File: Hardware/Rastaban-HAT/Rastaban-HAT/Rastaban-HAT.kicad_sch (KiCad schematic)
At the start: 59 parts, among them IC1 P82B96TD,118, J1 Screw_Terminal_01x04, J10 GPIO, J11 Conn_01x06_Male, J2 Screw_Terminal_01x04, J3 Screw_Terminal_01x04, J4 Screw_Terminal_01x02, J5 Jack-DC 12V+, J6 SM04B-SRSS-TB(LF)(SN), J7 Screw_Terminal_01x02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

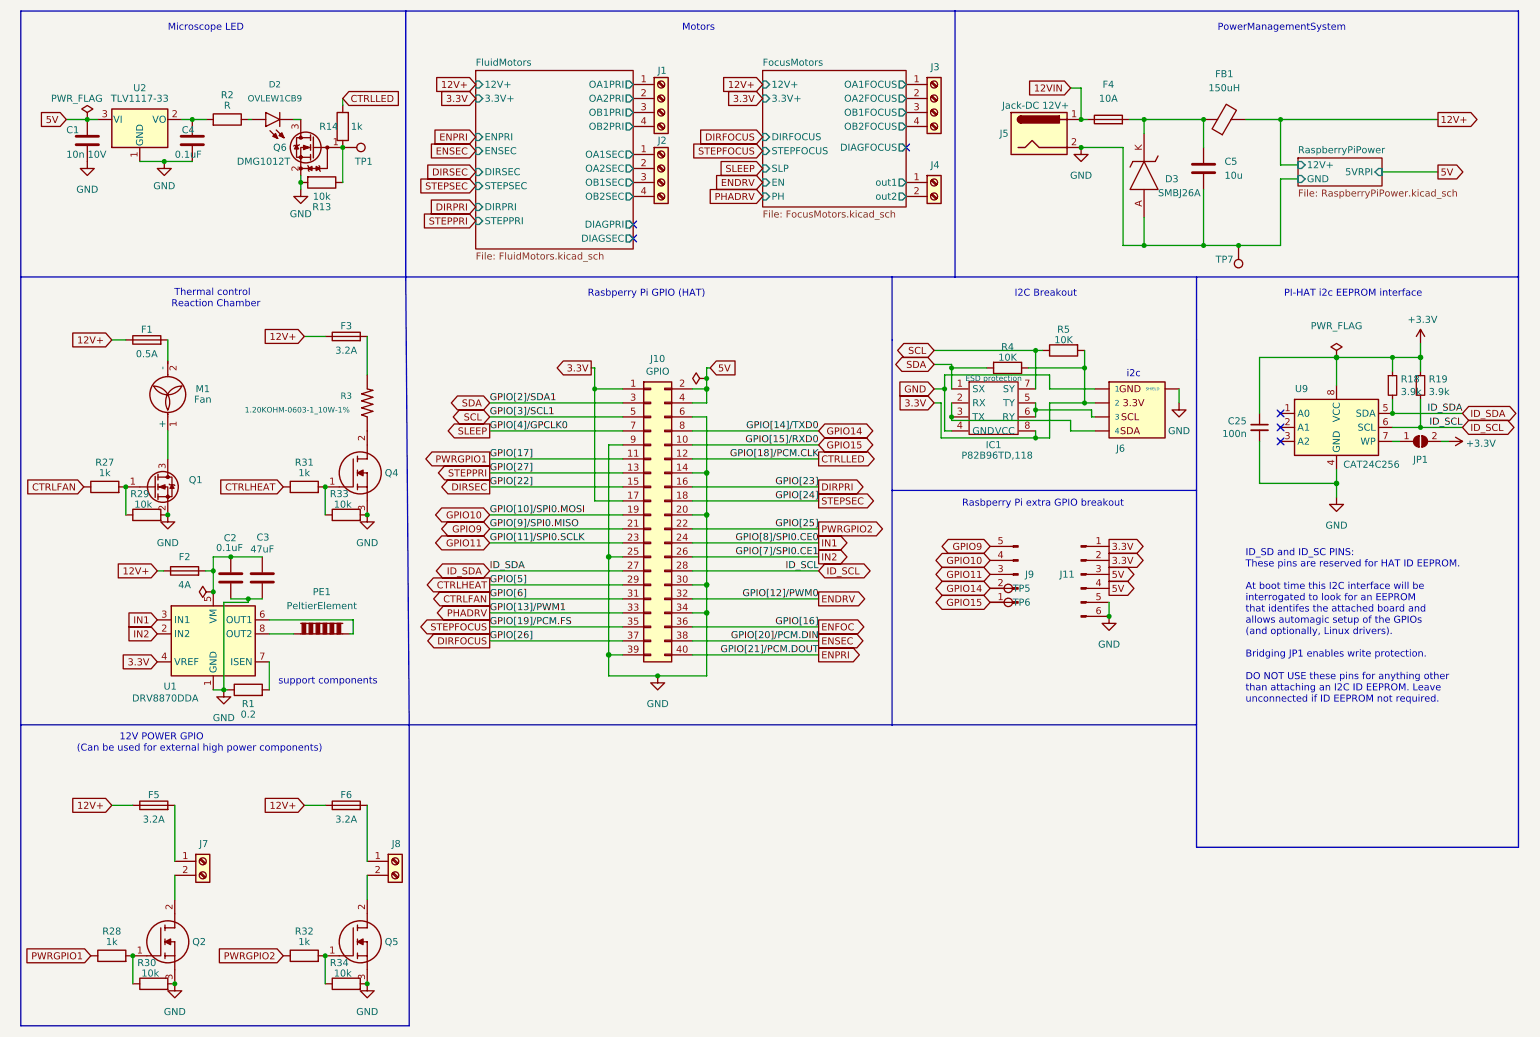
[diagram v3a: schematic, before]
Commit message: changed revision to v1.1 on all tabs
changed some capacitor values
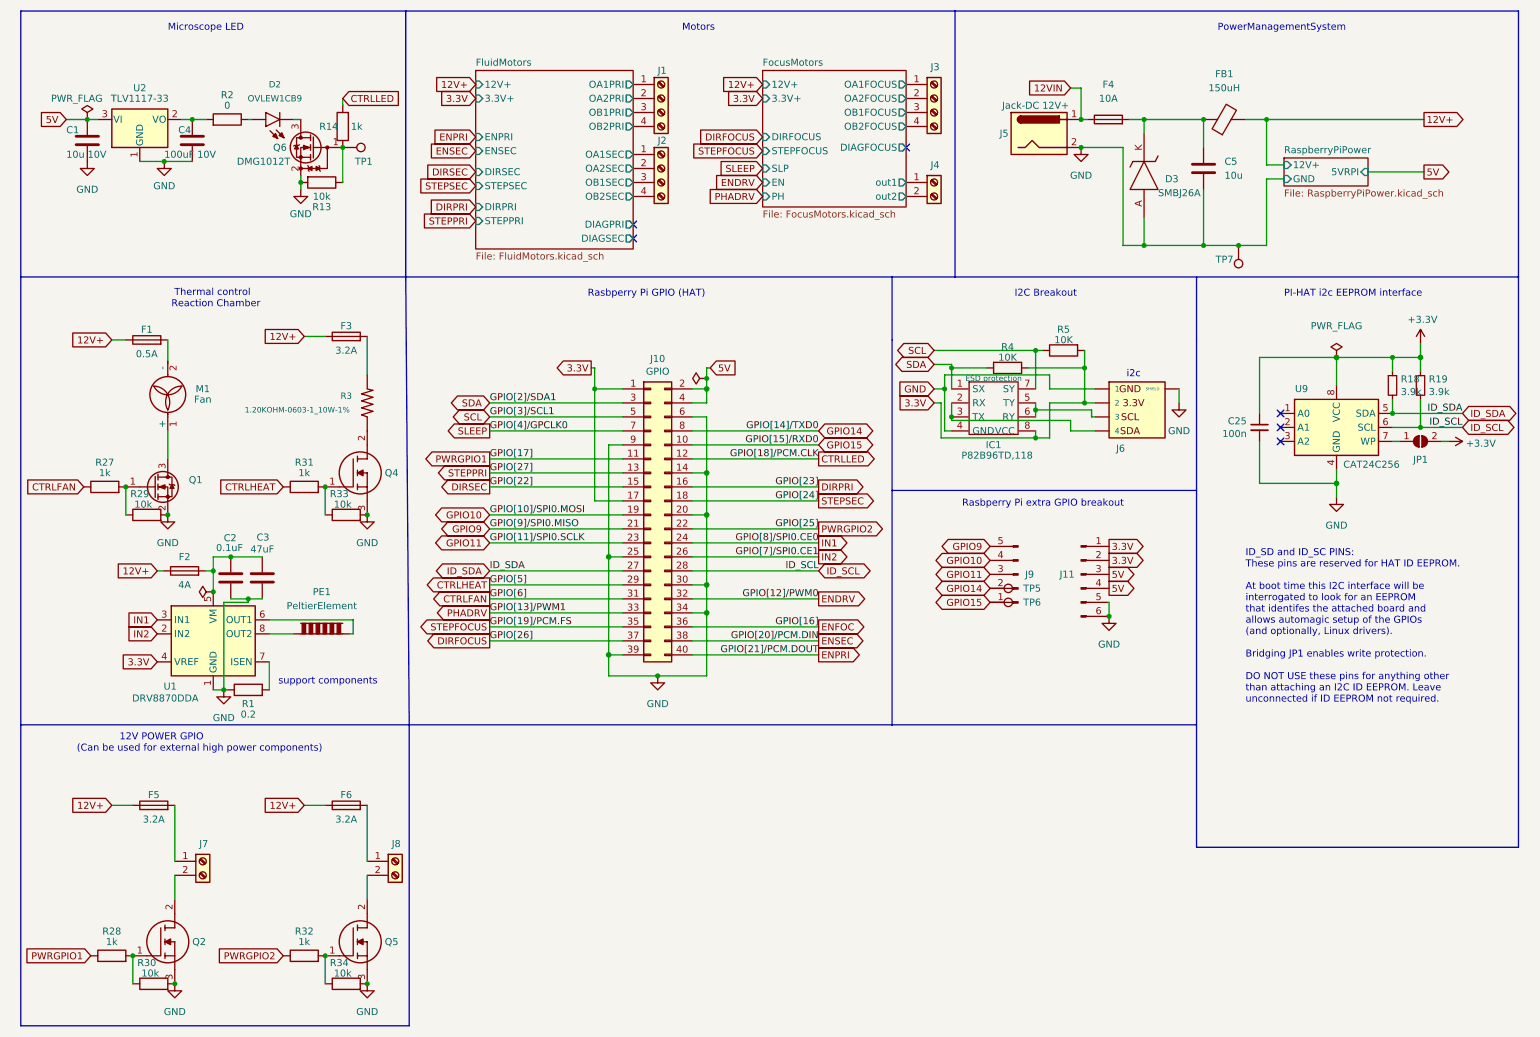
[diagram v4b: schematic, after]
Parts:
- C1: value 10n 10V -> 10u 10V
- C4: value 0.1uF -> 100uF 10V
- R2: value R -> 0
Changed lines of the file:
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@@
     (title "Rastaban-HAT")
     (date "2022-09-21")
-    (rev "1")
+    (rev "1.1")
     (company "HAN")
     (comment 1 "Casper R. Tak")
@@
   (junction (at 196.85 90.17) (diameter 0) (color 0 0 0 0)
   )
-  (junction (at 241.3 32.385) (diameter 0) (color 0 0 0 0)
+  (junction (at 238.76 32.385) (diameter 0) (color 0 0 0 0)
   )
   (junction (at 261.62 85.725) (diameter 0) (color 0 0 0 0)
@@
     (stroke (width 0) (type solid) (color 0 0 0 0))
   )
-  (wire (pts (xy 259.715 41.91) (xy 269.875 41.91))
+  (wire (pts (xy 257.175 41.91) (xy 267.335 41.91))
     (stroke (width 0) (type default) (color 0 0 0 0))
   )
@@
     (stroke (width 0) (type default) (color 0 0 0 0))
   )
-  (wire (pts (xy 241.3 43.18) (xy 244.475 43.18))
+  (wire (pts (xy 238.76 43.18) (xy 241.935 43.18))
     (stroke (width 0) (type default) (color 0 0 0 0))
   )
@@
     (stroke (width 0) (type default) (color 0 0 0 0))
   )
-  (wire (pts (xy 241.3 32.385) (xy 269.875 32.385))
+  (wire (pts (xy 238.76 32.385) (xy 267.335 32.385))
     (stroke (width 0) (type default) (color 0 0 0 0))
   )
@@
     (stroke (width 0) (type default) (color 0 0 0 0))
   )
+  (wire (pts (xy 234.95 32.385) (xy 238.76 32.385))
+    (stroke (width 0) (type default) (color 0 0 0 0))
+  )
   (wire (pts (xy 47.625 135.89) (xy 49.53 135.89))
     (stroke (width 0) (type default) (color 0 0 0 0))
@@
     (stroke (width 0) (type default) (color 0 0 0 0))
   )
-  (wire (pts (xy 233.68 55.245) (xy 241.3 55.245))
-    (stroke (width 0) (type default) (color 0 0 0 0))
-  )
   (wire (pts (xy 116.84 81.28) (xy 116.84 101.6))
     (stroke (width 0) (type solid) (color 0 0 0 0))
@@
     (stroke (width 0) (type default) (color 0 0 0 0))
   )
-  (wire (pts (xy 241.3 40.64) (xy 241.3 32.385))
+  (wire (pts (xy 238.76 40.64) (xy 238.76 32.385))
     (stroke (width 0) (type default) (color 0 0 0 0))
   )
@@
     (stroke (width 0) (type solid) (color 0 0 0 0))
   )
-  (wire (pts (xy 244.475 40.64) (xy 241.3 40.64))
+  (wire (pts (xy 241.935 40.64) (xy 238.76 40.64))
     (stroke (width 0) (type default) (color 0 0 0 0))
   )
@@
     (stroke (width 0) (type solid) (color 0 0 0 0))
   )
-  (wire (pts (xy 234.95 32.385) (xy 241.3 32.385))
-    (stroke (width 0) (type default) (color 0 0 0 0))
-  )
   (wire (pts (xy 119.38 133.35) (xy 128.27 133.35))
     (stroke (width 0) (type default) (color 0 0 0 0))
@@
     (stroke (width 0) (type solid) (color 0 0 0 0))
   )
+  (wire (pts (xy 233.68 55.245) (xy 238.76 55.245))
+    (stroke (width 0) (type default) (color 0 0 0 0))
+  )
   (polyline (pts (xy 12.7 12.7) (xy 12.7 60.96))
     (stroke (width 0) (type default) (color 0 0 0 0))
@@
     (stroke (width 0) (type solid) (color 0 0 0 0))
   )
+  (wire (pts (xy 227.33 55.245) (xy 233.68 55.245))
+    (stroke (width 0) (type default) (color 0 0 0 0))
+  )
   (wire (pts (xy 178.435 83.82) (xy 179.705 83.82))
     (stroke (width 0) (type default) (color 0 0 0 0))
@@
     (stroke (width 0) (type default) (color 0 0 0 0))
   )
-  (wire (pts (xy 227.33 55.245) (xy 233.68 55.245))
-    (stroke (width 0) (type default) (color 0 0 0 0))
-  )
   (wire (pts (xy 63.5 43.815) (xy 63.5 45.085))
     (stroke (width 0) (type default) (color 0 0 0 0))
@@
     (stroke (width 0) (type solid) (color 0 0 0 0))
   )
-  (wire (pts (xy 241.3 55.245) (xy 241.3 43.18))
+  (wire (pts (xy 238.76 55.245) (xy 238.76 43.18))
     (stroke (width 0) (type default) (color 0 0 0 0))
   )
@@
     )
   )
-  (global_label "5V" (shape output) (at 269.875 41.91 0) (fields_autoplaced)
+  (global_label "5V" (shape output) (at 267.335 41.91 0) (fields_autoplaced)
     (effects (font (size 1.27 1.27)) (justify left))
-    (property "Intersheet References" "${INTERSHEET_REFS}" (id 0) (at 274.5862 41.8306 0)
+    (property "Intersheet References" "${INTERSHEET_REFS}" (id 0) (at 272.0462 41.8306 0)
       (effects (font (size 1.27 1.27)) (justify left) hide)
     )
@@
     )
   )
-  (global_label "12V+" (shape output) (at 269.875 32.385 0) (fields_autoplaced)
+  (global_label "12V+" (shape output) (at 267.335 32.385 0) (fields_autoplaced)
     (effects (font (size 1.27 1.27)) (justify left))
-    (property "Intersheet References" "${INTERSHEET_REFS}" (id 0) (at 277.3681 32.3056 0)
+    (property "Intersheet References" "${INTERSHEET_REFS}" (id 0) (at 274.8281 32.3056 0)
       (effects (font (size 1.27 1.27)) (justify left) hide)
     )
@@
     (in_bom yes) (on_board yes)
     (property "Reference" "R2" (id 0) (at 50.165 27.94 90))
-    (property "Value" "R" (id 1) (at 50.165 29.845 90))
+    (property "Value" "0" (id 1) (at 50.165 29.845 90))
     (property "Footprint" "" (id 2) (at 50.165 34.163 90)
       (effects (font (size 1.27 1.27)) hide)
@@
   (symbol (lib_id "Connector:TestPoint") (at 188.595 117.475 270) (unit 1)
     (in_bom yes) (on_board yes)
-    (property "Reference" "TP5" (id 0) (at 194.31 117.475 90))
+    (property "Reference" "TP5" (id 0) (at 196.215 117.475 90))
     (property "Value" "TestPoint" (id 1) (at 193.675 117.475 0)
       (effects (font (size 1.27 1.27)) hide)
@@
   (symbol (lib_id "Connector:TestPoint") (at 188.595 120.015 270) (unit 1)
     (in_bom yes) (on_board yes)
-    (property "Reference" "TP6" (id 0) (at 194.31 120.015 90))
+    (property "Reference" "TP6" (id 0) (at 196.215 120.015 90))
     (property "Value" "TestPoint" (id 1) (at 193.675 120.015 0)
       (effects (font (size 1.27 1.27)) hide)
@@
   (symbol (lib_id "Device:C") (at 43.815 36.195 180) (unit 1)
     (in_bom yes) (on_board yes)
-    (property "Reference" "C4" (id 0) (at 41.91 34.29 0)
+    (property "Reference" "C4" (id 0) (at 41.275 34.29 0)
       (effects (font (size 1.27 1.27)) (justify right))
     )
-    (property "Value" "0.1uF" (id 1) (at 40.64 38.735 0)
+    (property "Value" "100uF 10V" (id 1) (at 38.735 38.735 0)
       (effects (font (size 1.27 1.27)) (justify right))
     )
@@
       (effects (font (size 1.27 1.27)) (justify left))
     )
-    (property "Value" "10n 10V" (id 1) (at 20.955 38.735 0)
+    (property "Value" "10u 10V" (id 1) (at 20.955 38.735 0)
       (effects (font (size 1.27 1.27)) (justify left))
     )
@@
     )
   )
-  (sheet (at 244.475 39.37) (size 15.24 5.08) (fields_autoplaced)
+  (sheet (at 241.935 39.37) (size 15.24 5.08) (fields_autoplaced)
     (stroke (width 0.1524) (type solid) (color 0 0 0 0))
     (fill (color 0 0 0 0.0000))
-    (property "Sheet name" "RaspberryPiPower" (id 0) (at 244.475 38.6584 0)
+    (property "Sheet name" "RaspberryPiPower" (id 0) (at 241.935 38.6584 0)
       (effects (font (size 1.27 1.27)) (justify left bottom))
     )
-    (property "Sheet file" "RaspberryPiPower.kicad_sch" (id 1) (at 244.475 45.0346 0)
+    (property "Sheet file" "RaspberryPiPower.kicad_sch" (id 1) (at 241.935 45.0346 0)
       (effects (font (size 1.27 1.27)) (justify left top))
     )
-    (pin "12V+" input (at 244.475 40.64 180)
+    (pin "12V+" input (at 241.935 40.64 180)
       (effects (font (size 1.27 1.27)) (justify left))
     )
-    (pin "GND" input (at 244.475 43.18 180)
+    (pin "GND" input (at 241.935 43.18 180)
       (effects (font (size 1.27 1.27)) (justify left))
     )
-    (pin "5VRPI" input (at 259.715 41.91 0)
+    (pin "5VRPI" input (at 257.175 41.91 0)
       (effects (font (size 1.27 1.27)) (justify right))
     )
@@
     )
     (path "/f3fe5026-3ec3-4ef9-8ee4-ac53381f5d3c"
-      (reference "C1") (unit 1) (value "10n 10V") (footprint "")
+      (reference "C1") (unit 1) (value "10u 10V") (footprint "")
     )
     (path "/6e705e76-606c-4ed6-ae7f-ed966b630818"
@@
     )
     (path "/9f7db502-d21d-4e3f-97d2-a5c274cc55fe"
-      (reference "C4") (unit 1) (value "0.1uF") (footprint "Capacitor_SMD:C_1206_3216Metric_Pad1.33x1.80mm_HandSolder")
+      (reference "C4") (unit 1) (value "100uF 10V") (footprint "Capacitor_SMD:C_1206_3216Metric_Pad1.33x1.80mm_HandSolder")
     )
     (path "/bf4c234e-8821-4f3f-91ed-c4127b83d67d"
@@
     )
     (path "/509754cd-dbf1-46e6-965c-38d41c0b6924/b391f05e-9d79-4808-8c88-d0da93b38ae2"
-      (reference "C16") (unit 1) (value "100n 35V") (footprint "")
+      (reference "C16") (unit 1) (value "100u 35V") (footprint "")
     )
     (path "/509754cd-dbf1-46e6-965c-38d41c0b6924/e00c426b-f72a-4212-94e0-d9ce7621402d"
-      (reference "C17") (unit 1) (value "100n 35V") (footprint "")
+      (reference "C17") (unit 1) (value "100u 35V") (footprint "")
     )
     (path "/7b03732c-6b0a-482e-b8e3-ced6ad7436b5/6a92e50c-ed6c-499b-95da-e3221c59e174"
@@
     )
     (path "/7b03732c-6b0a-482e-b8e3-ced6ad7436b5/e5d64b5c-b610-4e2e-9355-8b38ef775df4"
-      (reference "C19") (unit 1) (value "10n 10V") (footprint "")
+      (reference "C19") (unit 1) (value "10u 10V") (footprint "")
     )
     (path "/6d1772b3-b434-4c39-820a-75c27b63c8e3"
@@
     )
     (path "/00db92f9-b335-411c-b323-c06099a8c80d"
-      (reference "R2") (unit 1) (value "R") (footprint "")
+      (reference "R2") (unit 1) (value "0") (footprint "")
     )
     (path "/e2569925-ebf9-4052-bd02-8582502d3183"

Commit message: Heavily improved symbol text placements
all texts are now readable
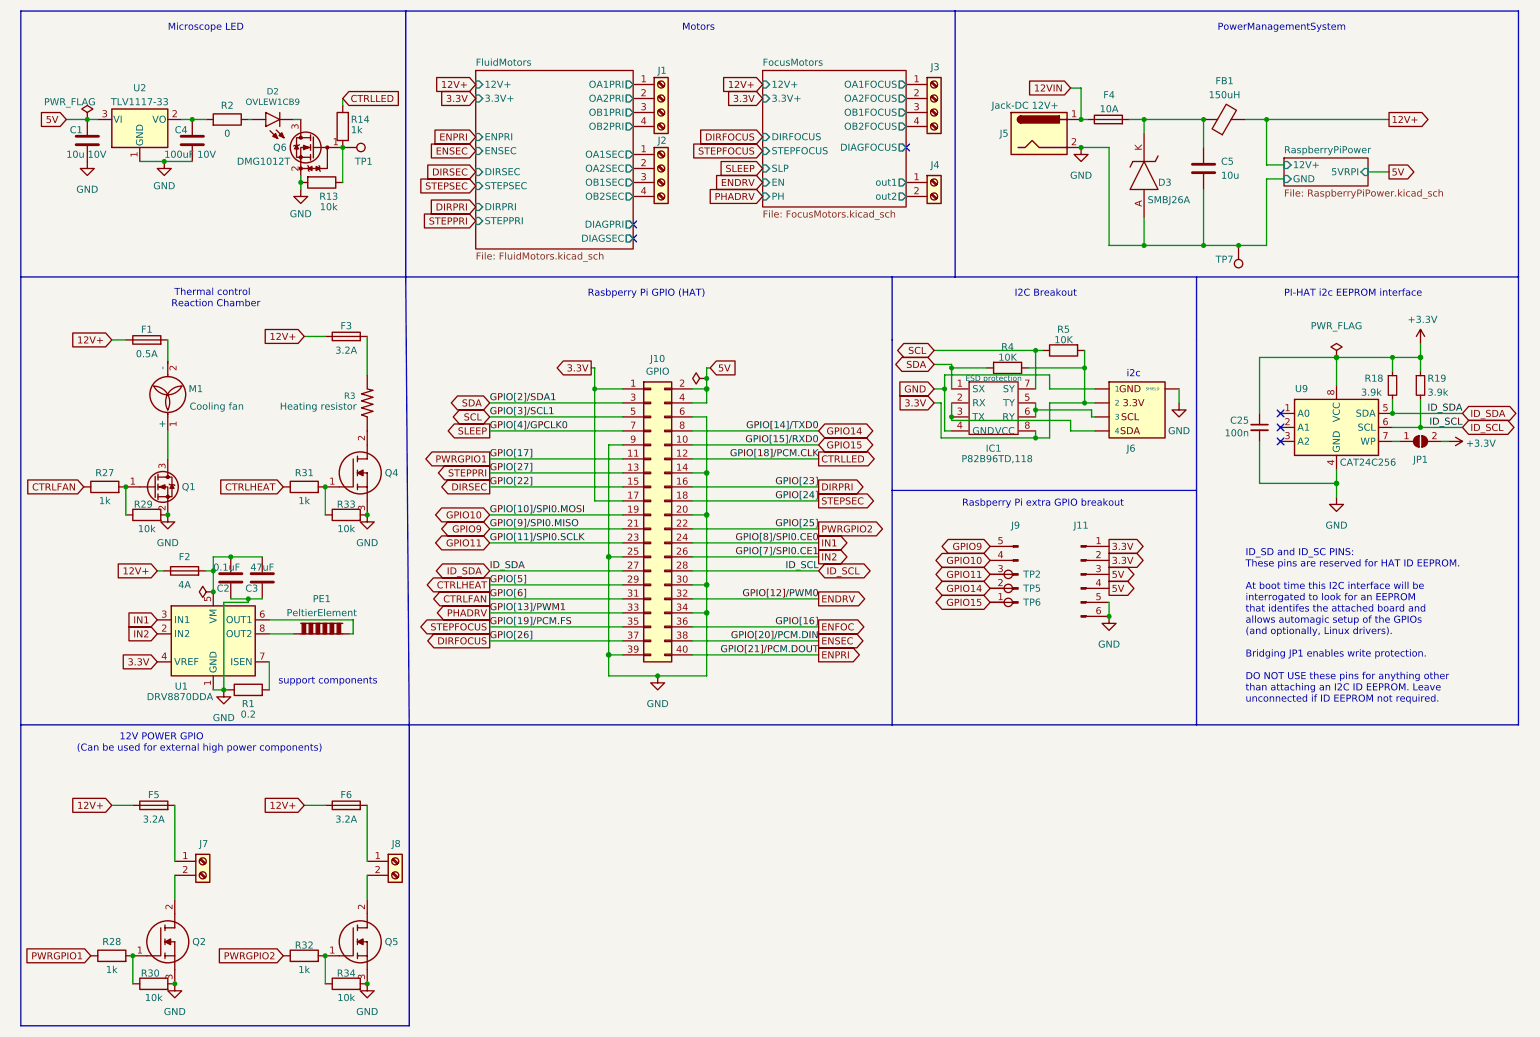
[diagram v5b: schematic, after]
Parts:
- added TP2: TestPoint, TestPoint:TestPoint_Bridge_Pitch7.62mm_Drill1.3mm, symbol Connector:TestPoint
- M1: Purpose (none) -> Cooling fan
- R3: Purpose (none) -> Heating resistor
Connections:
- net GPIO11: now also TP2.1
